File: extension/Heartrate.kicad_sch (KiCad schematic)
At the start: 27 parts, among them IC501 MAX32664, IC502 LIS2DS12, IC503 MAX86141, U501 MAX4740ETE+, Y501 32kHz

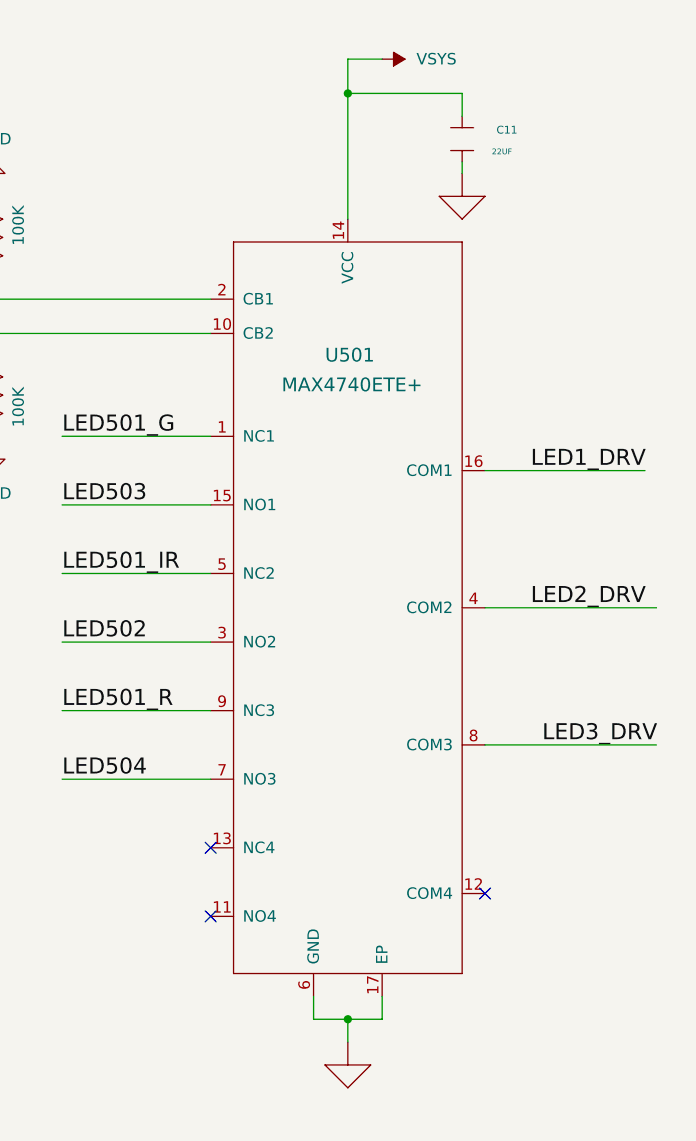
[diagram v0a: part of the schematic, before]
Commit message: update-lookup table, fix ERC GND error
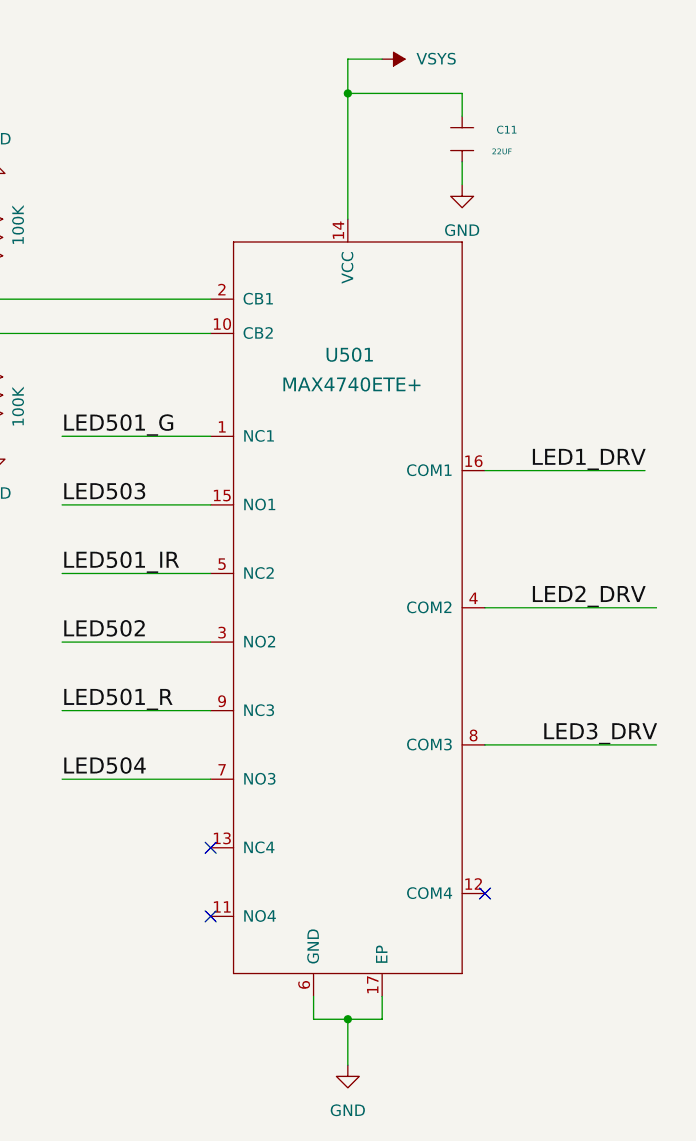
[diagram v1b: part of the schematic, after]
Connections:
- net GND_SIGNAL is gone; now on net GND: C11.1, U501.17 (EP), U501.6 (GND)

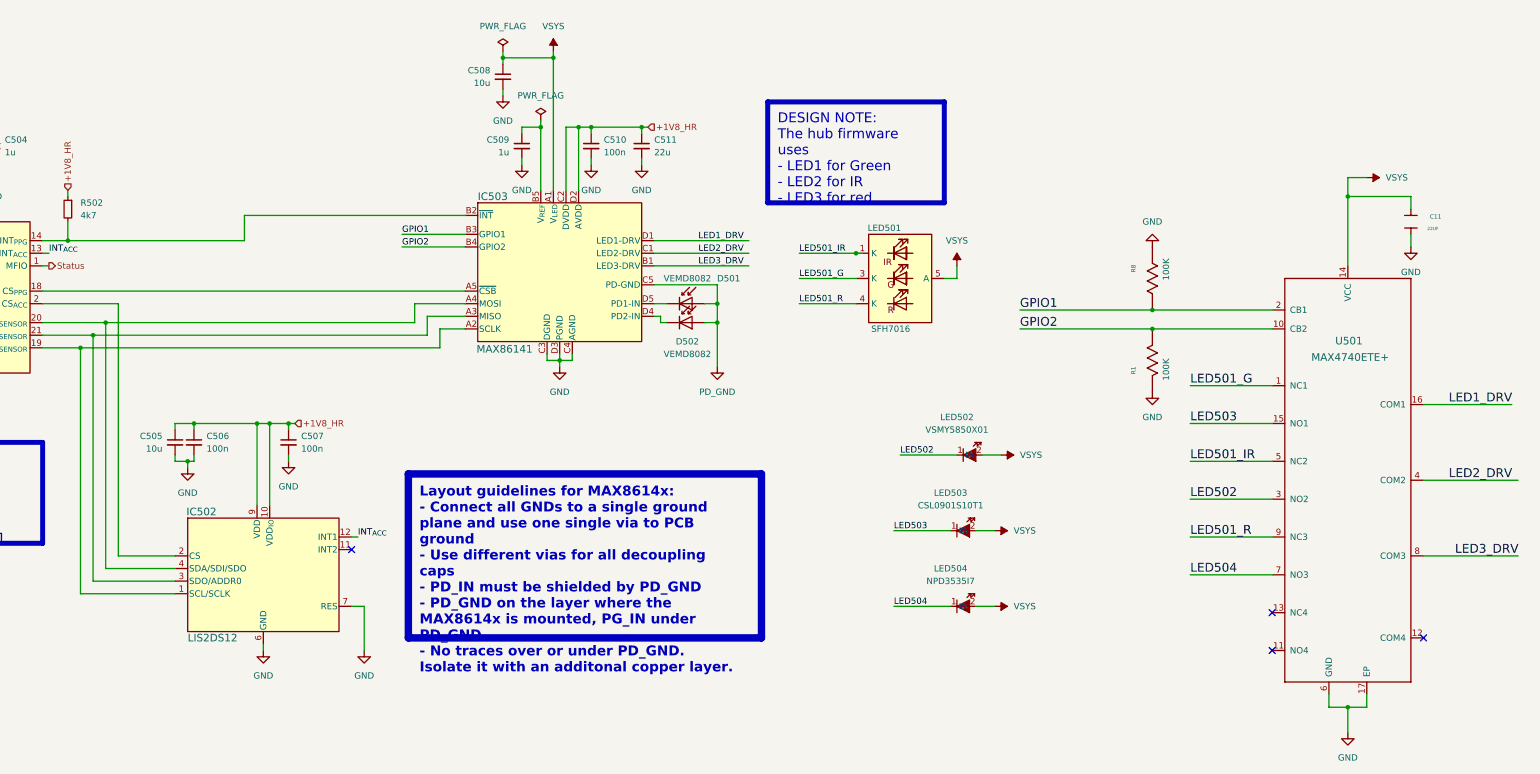
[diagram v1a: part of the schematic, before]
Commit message: change MUX from MAX4740 to MAX14778
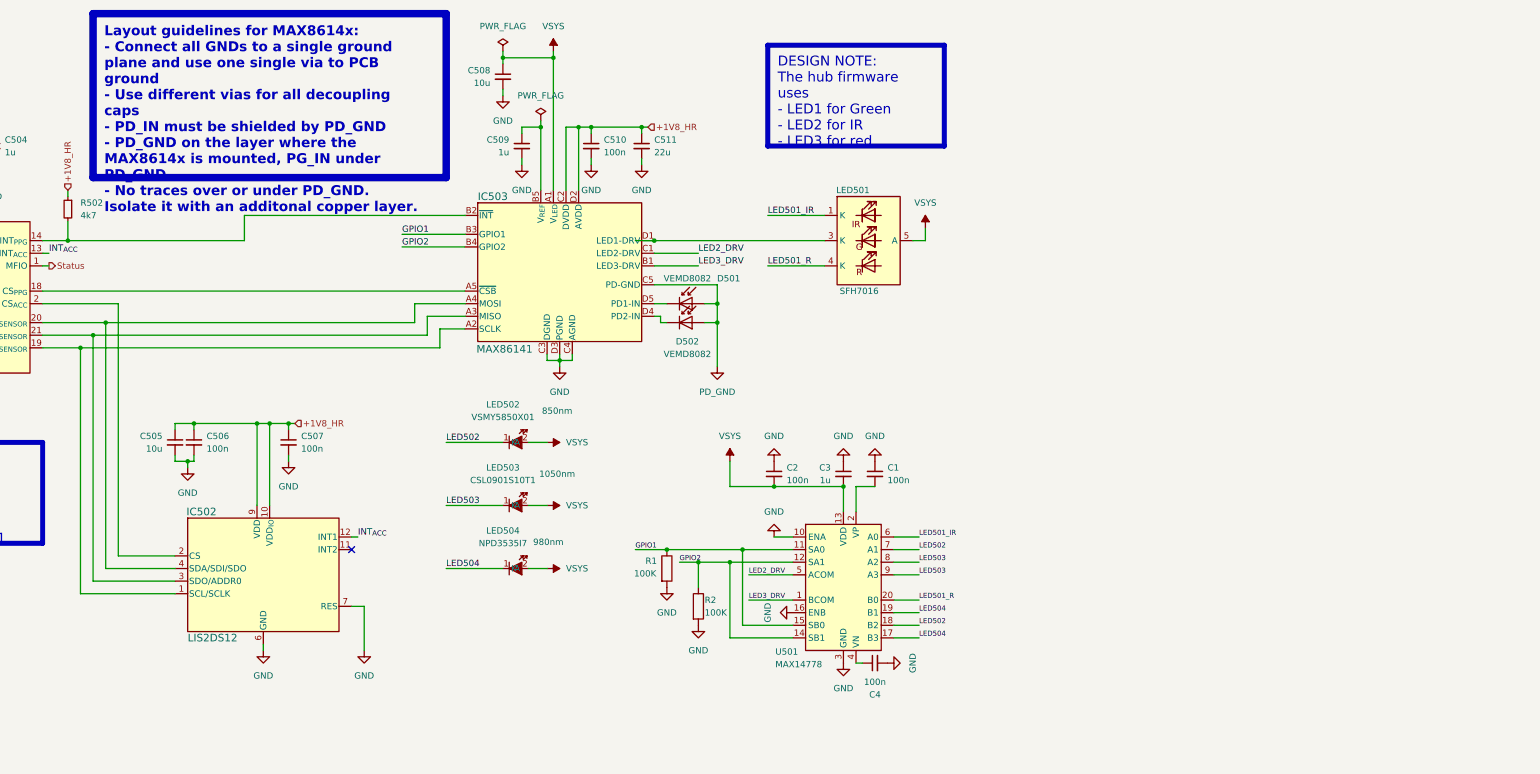
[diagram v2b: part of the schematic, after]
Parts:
- removed C11: 22UF, MRD103_SENSRBRD_APPS:0402, symbol MRD103_SENSRBRD_APPS-lib:CAP_NP
- removed R1, R8: 100K, MRD103_SENSRBRD_APPS:RESC1005X50L, symbol MRD103_SENSRBRD_APPS-lib:EK_RES_SMDEK_RES_SMD
- removed U501: MAX4740ETE+, MRD103_SENSRBRD_APPS:MAXIM_90-0031, symbol MRD103_SENSRBRD_APPS-lib:MAX4740
- added C1, C2, C4: 100n, Capacitor_SMD:C_0201_0603Metric, symbol Device:C_Small
- added C3: 1u, Capacitor_SMD:C_0201_0603Metric, symbol Device:C_Small
- added R1, R2: 100K, symbol Device:R
- added U501: MAX14778, Package_DFN_QFN:TQFN-20-1EP_5x5mm_P0.65mm_EP3.1x3.1mm, symbol Analog_Switch:MAX14778
- LED502: Wavelength_nm 850 -> 850nm
- LED503: Wavelength_nm 1050 -> 1050nm
- LED504: Wavelength_nm 980 -> 980nm
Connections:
- net LED501_G is gone; now on an unnamed net: LED501.3 (K)
- net GND: now also C1.1, C2.1, C3.1, C4.2, R1.2, R2.2, U501.10 (ENA), U501.16 (ENB), U501.3 (GND)
- net GPIO1: now also R1.1, U501.11 (SA0), U501.15 (SB0)
- net GPIO2: now also R2.1, U501.12 (SA1), U501.14 (SB1)
- net LED2_DRV: now also U501.5 (ACOM)
- net LED3_DRV: now also U501.1 (BCOM)
- net LED501_IR: now also U501.6 (A0)
- net LED501_R: now also U501.20 (B0)
- net LED502: now also U501.18 (B2), U501.7 (A1)
- net LED503: now also U501.8 (A2), U501.9 (A3)
- net LED504: now also U501.17 (B3), U501.19 (B1)
- net VSYS: now also C2.2, C3.2, U501.13 (VDD)
- net LED1_DRV: no longer names the net of IC503.D1 (LED1-DRV)
- new net: C1.2, U501.2 (VP)
- new net: C4.1, U501.21 (VN), U501.4 (VN)
- no-connect marks 4 -> 1
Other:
- moved on the sheet: LED501, LED502, LED503, LED504

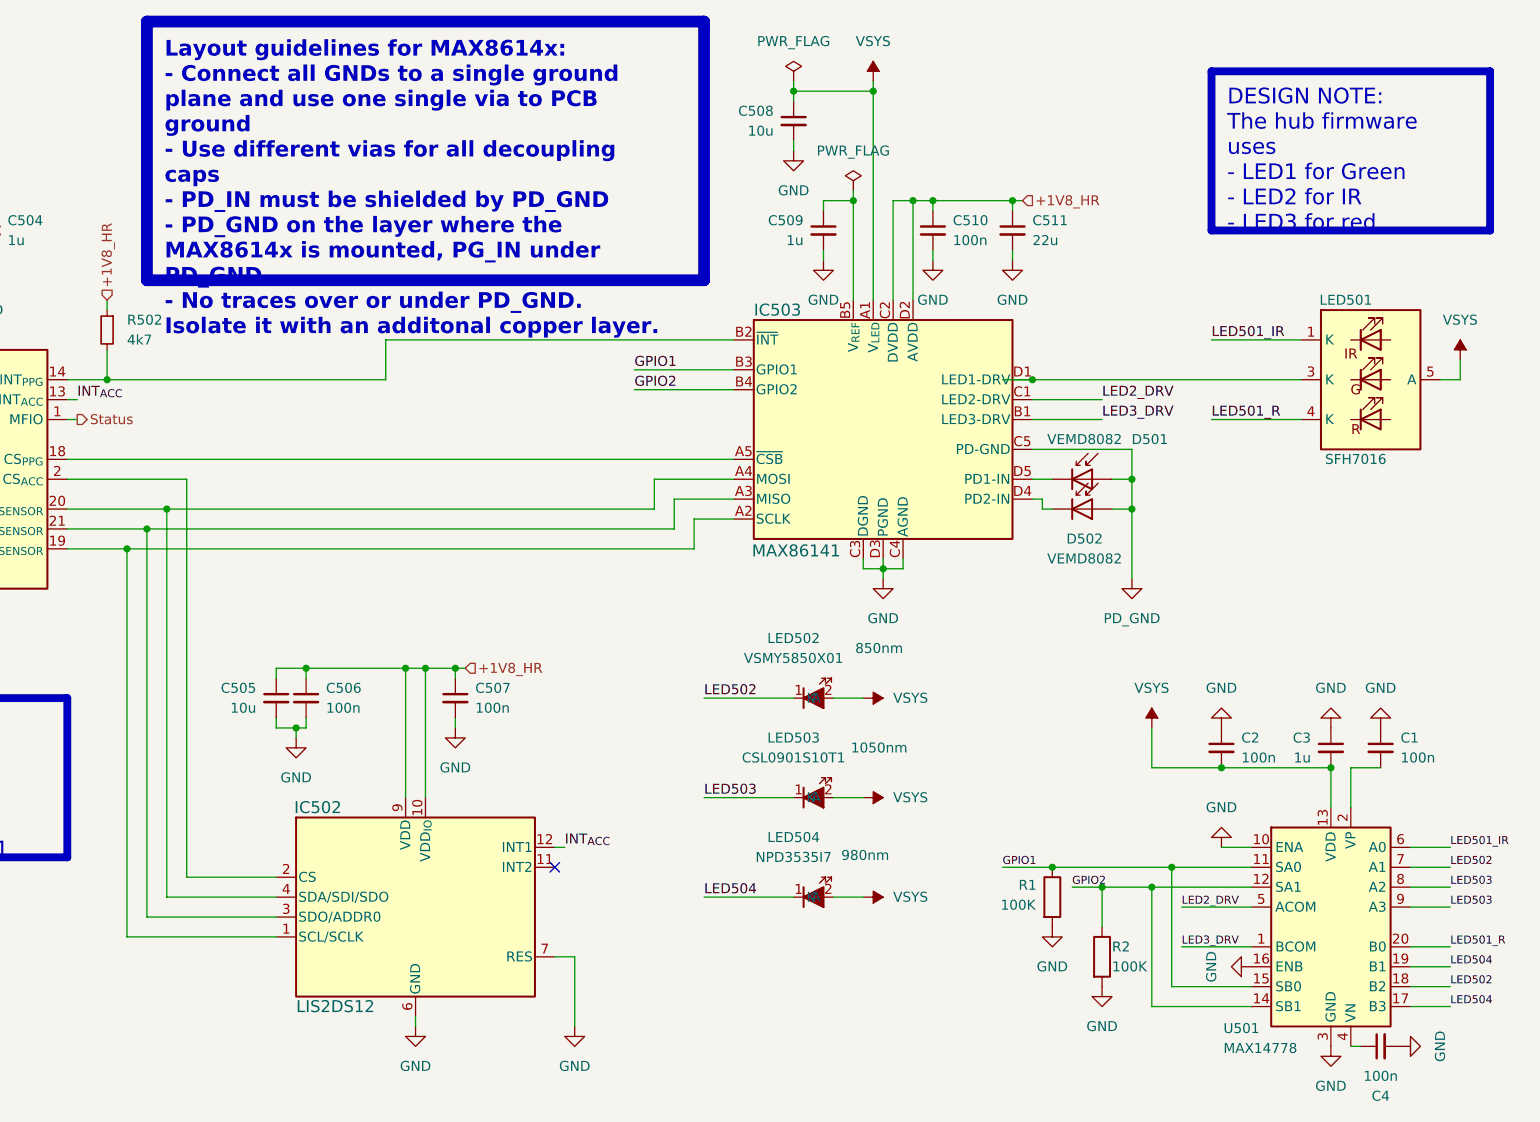
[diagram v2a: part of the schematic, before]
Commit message: try to fix MUX - ENA and ENB
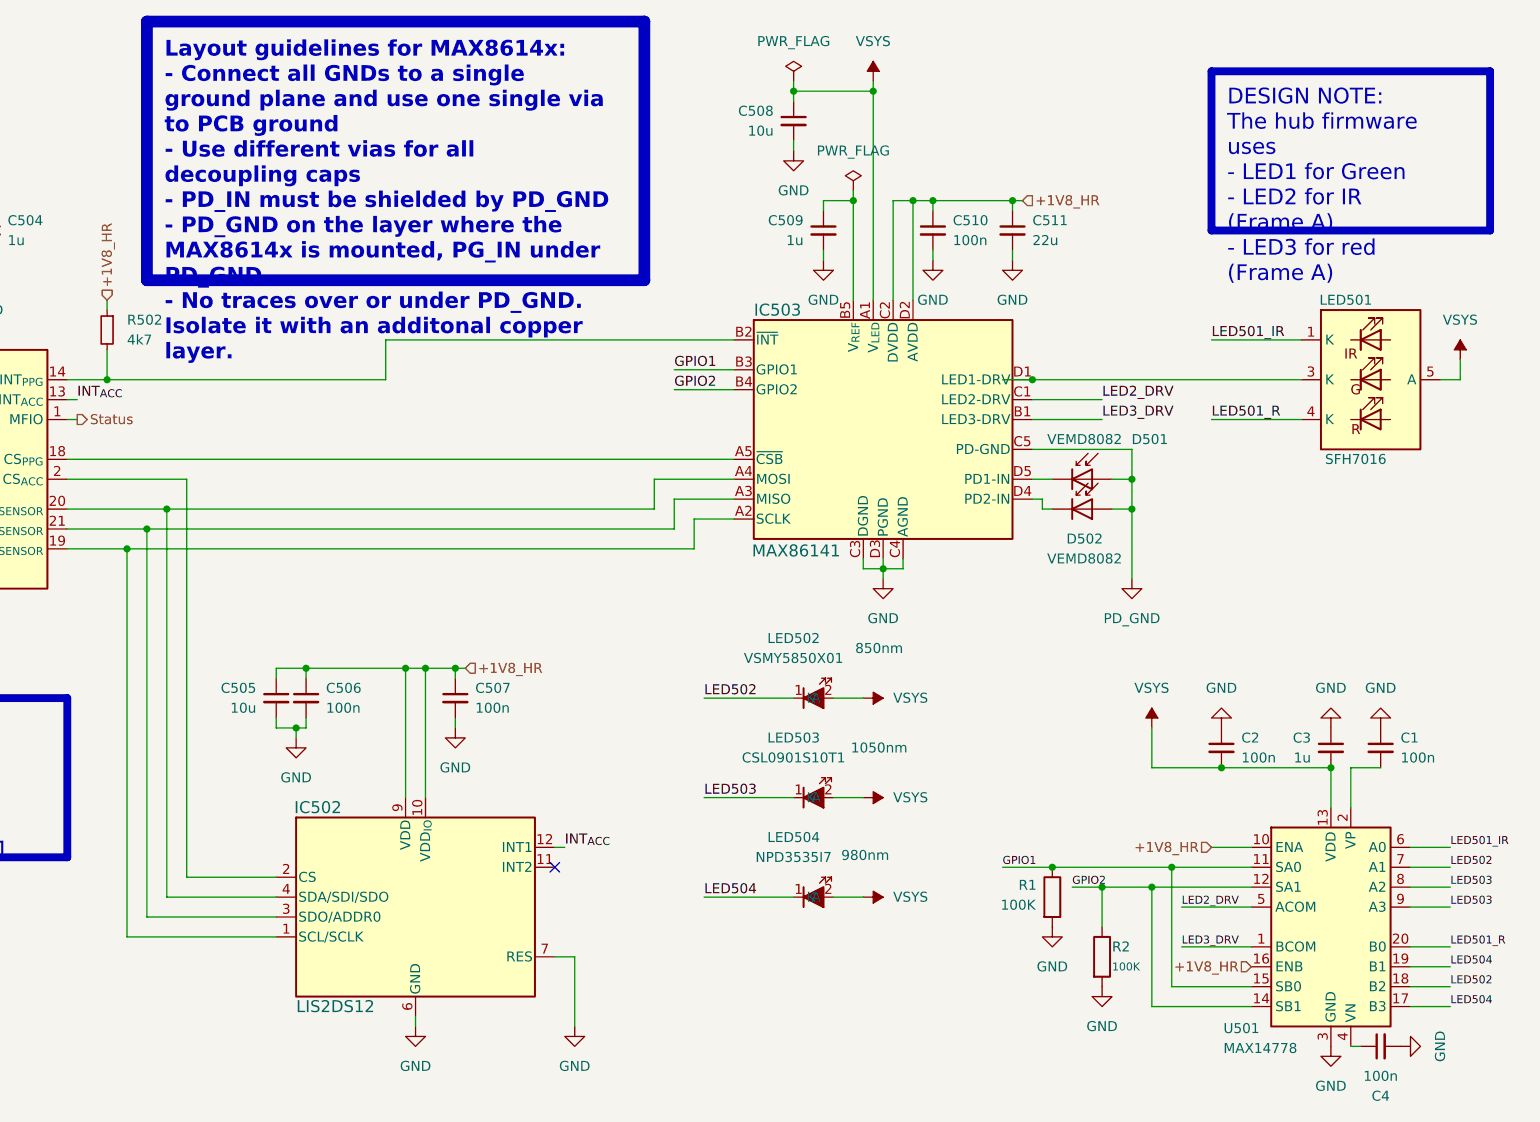
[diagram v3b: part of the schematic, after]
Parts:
- R1, R2: footprint (none) -> Resistor_SMD:R_0402_1005Metric
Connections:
- net +1V8_HR: now also U501.10 (ENA), U501.16 (ENB)
- net GND: no longer U501.10 (ENA), U501.16 (ENB)
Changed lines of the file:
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@@
 		)
 	)
-	(text_box "DESIGN NOTE:\nThe hub firmware uses\n- LED1 for Green\n- LED2 for IR\n- LED3 for red"
+	(text_box "DESIGN NOTE:\nThe hub firmware uses\n- LED1 for Green\n- LED2 for IR (Frame A)\n- LED3 for red (Frame A)"
 		(exclude_from_sim no)
 		(at 242.57 20.32 0)
@@
 		(exclude_from_sim no)
 		(at 106.68 13.97 0)
-		(size 71.12 33.02)
+		(size 63.5 33.02)
 		(margins 2.25 2.25 2.25 2.25)
 		(stroke
@@
 	(wire
 		(pts
-			(xy 168.91 58.42) (xy 181.61 58.42)
+			(xy 173.99 58.42) (xy 181.61 58.42)
 		)
 		(stroke
@@
 	(wire
 		(pts
-			(xy 168.91 60.96) (xy 181.61 60.96)
+			(xy 173.99 60.96) (xy 181.61 60.96)
 		)
 		(stroke
@@
 	(wire
 		(pts
+			(xy 234.95 124.46) (xy 234.95 139.7)
+		)
+		(stroke
+			(width 0)
+			(type default)
+		)
+	)
+	(wire
+		(pts
 			(xy 228.6 124.46) (xy 228.6 129.54)
 		)
@@
 	(wire
 		(pts
+			(xy 242.57 119.38) (xy 247.65 119.38)
+		)
+		(stroke
+			(width 0)
+			(type default)
+		)
+	)
+	(wire
+		(pts
 			(xy 158.75 119.38) (xy 160.02 119.38)
 		)
@@
 	(wire
 		(pts
-			(xy 243.84 119.38) (xy 247.65 119.38)
-		)
-		(stroke
-			(width 0)
-			(type default)
-		)
-	)
-	(wire
-		(pts
 			(xy 171.45 76.2) (xy 171.45 72.39)
 		)
@@
 	(wire
 		(pts
-			(xy 234.95 124.46) (xy 234.95 139.7)
-		)
-		(stroke
-			(width 0)
-			(type default)
-		)
-	)
-	(wire
-		(pts
 			(xy 198.12 83.82) (xy 200.66 83.82)
 		)
@@
 	)
 	(image
-		(at 189.23 140.97)
+		(at 191.77 142.24)
 		(scale 1.31273)
 		(data "/9j/4AAQSkZJRgABAQAAAQABAAD/4gHYSUNDX1BST0ZJTEUAAQEAAAHIAAAAAAQwAABtbnRyUkdC"
@@
 	)
 	(label "GPIO2"
-		(at 168.91 60.96 0)
+		(at 173.99 60.96 0)
 		(effects
 			(font
@@
 	)
 	(label "GPIO1"
-		(at 168.91 58.42 0)
+		(at 173.99 58.42 0)
 		(effects
 			(font
@@
 	(hierarchical_label "+1V8_HR"
 		(shape input)
+		(at 242.57 119.38 180)
+		(effects
+			(font
+				(size 1.27 1.27)
+			)
+			(justify right)
+		)
+	)
+	(hierarchical_label "+1V8_HR"
+		(shape input)
 		(at 218.44 36.83 0)
 		(effects
@@
 		)
 	)
+	(hierarchical_label "+1V8_HR"
+		(shape input)
+		(at 247.65 134.62 180)
+		(effects
+			(font
+				(size 1.27 1.27)
+			)
+			(justify right)
+		)
+	)
 	(symbol
 		(lib_id "power:GND")
@@
 	)
 	(symbol
-		(lib_id "power:GND")
-		(at 247.65 134.62 270)
-		(mirror x)
-		(unit 1)
-		(exclude_from_sim no)
-		(in_bom yes)
-		(on_board yes)
-		(dnp no)
-		(property "Reference" "#PWR010"
-			(at 241.3 134.62 0)
-			(effects
-				(font
-					(size 1.27 1.27)
-				)
-				(hide yes)
-			)
-		)
-		(property "Value" "GND"
-			(at 242.57 134.62 0)
-			(effects
-				(font
-					(size 1.27 1.27)
-				)
-			)
-		)
-		(property "Footprint" ""
-			(at 247.65 134.62 0)
-			(effects
-				(font
-					(size 1.27 1.27)
-				)
-				(hide yes)
-			)
-		)
-		(property "Datasheet" ""
-			(at 247.65 134.62 0)
-			(effects
-				(font
-					(size 1.27 1.27)
-				)
-				(hide yes)
-			)
-		)
-		(property "Description" "Power symbol creates a global label with name \"GND\" , ground"
-			(at 247.65 134.62 0)
-			(effects
-				(font
-					(size 1.27 1.27)
-				)
-				(hide yes)
-			)
-		)
-		(pin "1"
-		)
-		(instances
-			(project "ZSWatch-Extension"
-				(path "/d5742f03-3b1a-42e5-a384-018bd4b919aa/c5103ceb-5325-4a84-a025-9638a412984e/82af773f-8c39-43b9-baa2-3658da6c8bb2"
-					(reference "#PWR010")
-					(unit 1)
-				)
-			)
-		)
-	)
-	(symbol
 		(lib_id "power:PWR_FLAG")
 		(at 196.85 35.56 0)
@@
 			)
 		)
-		(property "Footprint" ""
+		(property "Footprint" "Resistor_SMD:R_0402_1005Metric"
 			(at 220.472 125.73 90)
 			(effects
@@
 			(effects
 				(font
-					(size 1.27 1.27)
+					(size 1.016 1.016)
 				)
 				(justify left)
 			)
 		)
-		(property "Footprint" ""
+		(property "Footprint" "Resistor_SMD:R_0402_1005Metric"
 			(at 226.822 133.35 90)
 			(effects
@@
 					(unit 1)
 				)
-			)
-		)
-	)
-	(symbol
-		(lib_id "power:GND")
-		(at 243.84 119.38 0)
-		(mirror x)
-		(unit 1)
-		(exclude_from_sim no)
-		(in_bom yes)
-		(on_board yes)
-		(dnp no)
-		(property "Reference" "#PWR09"
-			(at 243.84 113.03 0)
-			(effects
-				(font
-					(size 1.27 1.27)
-				)
-				(hide yes)
-			)
-		)
-		(property "Value" "GND"
-			(at 243.84 114.3 0)
-			(effects
-				(font
-					(size 1.27 1.27)
-				)
-			)
-		)
-		(property "Footprint" ""
-			(at 243.84 119.38 0)
-			(effects
-				(font
-					(size 1.27 1.27)
-				)
-				(hide yes)
-			)
-		)
-		(property "Datasheet" ""
-			(at 243.84 119.38 0)
-			(effects
-				(font
-					(size 1.27 1.27)
-				)
-				(hide yes)
-			)
-		)
-		(property "Description" "Power symbol creates a global label with name \"GND\" , ground"
-			(at 243.84 119.38 0)
-			(effects
-				(font
-					(size 1.27 1.27)
-				)
-				(hide yes)
-			)
-		)
-		(pin "1"
-		)
-		(instances
-			(project "ZSWatch-Extension"
-				(path "/d5742f03-3b1a-42e5-a384-018bd4b919aa/c5103ceb-5325-4a84-a025-9638a412984e/82af773f-8c39-43b9-baa2-3658da6c8bb2"
-					(reference "#PWR09")
-					(unit 1)
-				)
